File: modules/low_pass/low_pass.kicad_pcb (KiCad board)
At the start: 2 copper layers, 30.5 x 68.6 mm, 4 parts

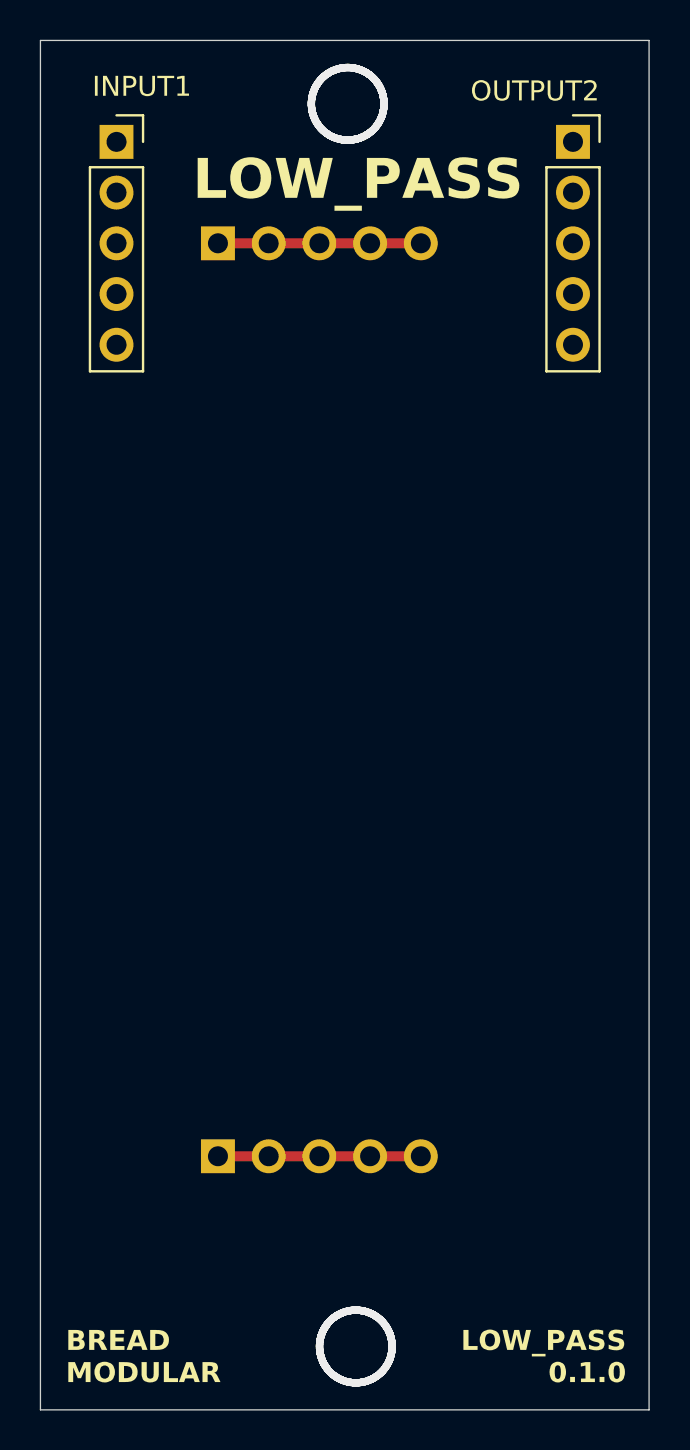
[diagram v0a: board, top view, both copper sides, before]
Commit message: layout components in the PCB
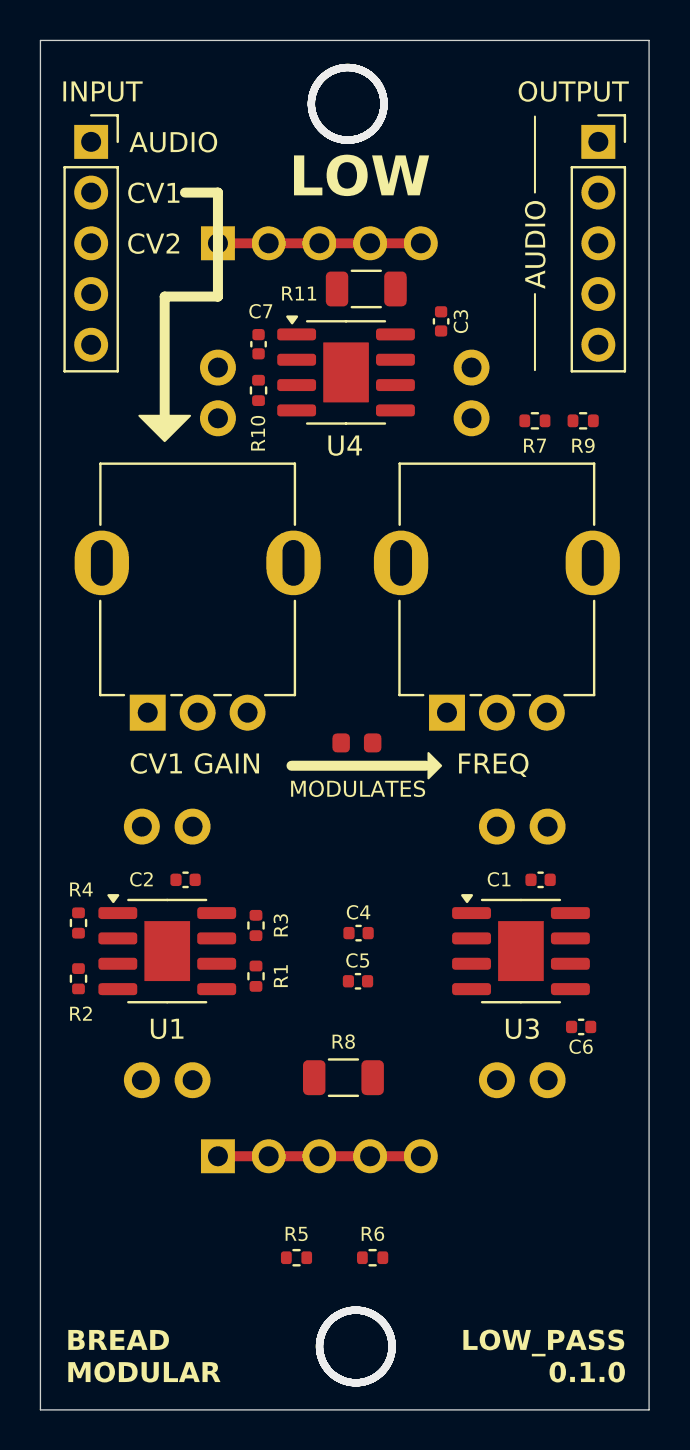
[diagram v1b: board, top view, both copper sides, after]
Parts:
- removed OUTPUT2: Conn_01x05_Socket, Connector_PinSocket_2.54mm:PinSocket_1x05_P2.54mm_Vertical
- added C1: 0.1uf, Capacitor_SMD:C_0402_1005Metric, F.Cu at (72.0, 82.7)
- added C2: 0.1uf, Capacitor_SMD:C_0402_1005Metric, F.Cu at (54.3, 82.7)
- added C3: 0.1uf, Capacitor_SMD:C_0402_1005Metric, F.Cu at (67.1, 54.7)
- added C4: 1nf, Capacitor_SMD:C_0402_1005Metric, F.Cu at (62.9, 85.3)
- added C5: 1nf, Capacitor_SMD:C_0402_1005Metric, F.Cu at (62.9, 87.8)
- added C6: 1nf, Capacitor_SMD:C_0402_1005Metric, F.Cu at (74.1, 90.0)
- added C7: 0.1uf, Capacitor_SMD:C_0402_1005Metric, F.Cu at (57.9, 55.9)
- added D1: LED, LED_SMD:LED_0603_1608Metric, F.Cu at (62.8, 75.8)
- added OUTPUT1: Conn_01x05_Socket, Connector_PinSocket_2.54mm:PinSocket_1x05_P2.54mm_Vertical, F.Cu at (74.9, 45.7)
- added R1: 100k, Resistor_SMD:R_0402_1005Metric, F.Cu at (57.8, 87.5)
- added R10: 100k, Resistor_SMD:R_0402_1005Metric, F.Cu at (57.9, 58.2)
- added R11: 330, Resistor_SMD:R_1206_3216Metric, F.Cu at (63.3, 53.1)
- added R2: 100k, Resistor_SMD:R_0402_1005Metric, F.Cu at (48.9, 87.6)
- added R3: 100k, Resistor_SMD:R_0402_1005Metric, F.Cu at (57.8, 85.0)
- added R4: 200k, Resistor_SMD:R_0402_1005Metric, F.Cu at (48.9, 84.8)
- added R5: 1k, Resistor_SMD:R_0402_1005Metric, F.Cu at (59.8, 101.6)
- added R6: 1k, Resistor_SMD:R_0402_1005Metric, F.Cu at (63.6, 101.6)
- added R7: 100k, Resistor_SMD:R_0402_1005Metric, F.Cu at (71.8, 59.7)
- added R8: 330, Resistor_SMD:R_1206_3216Metric, F.Cu at (62.2, 92.6)
- added R9: 1k, Resistor_SMD:R_0402_1005Metric, F.Cu at (74.2, 59.7)
- added RV1: 1M, BreadModular_Pots:Potentiometer_RV09, F.Cu at (52.4, 74.3)
- added RV2: 1M, BreadModular_Pots:Potentiometer_RV09, F.Cu at (67.3, 74.3)
- added U1: MCP6002-xSN, Package_SO:SOIC-8-1EP_3.9x4.9mm_P1.27mm_EP2.29x3mm, F.Cu at (53.3, 86.2)
- added U2: VTL5C, BreadModular_MISC:VTL5C, B.Cu at (71.1, 86.4)
- added U3: MCP6002-xSN, Package_SO:SOIC-8-1EP_3.9x4.9mm_P1.27mm_EP2.29x3mm, F.Cu at (71.1, 86.2)
- added U4: MCP6002-xSN, Package_SO:SOIC-8-1EP_3.9x4.9mm_P1.27mm_EP2.29x3mm, F.Cu at (62.3, 57.3)
- added U5: VTL5C, BreadModular_MISC:VTL5C, B.Cu at (53.3, 86.4)
- added U6: VTL5C, BreadModular_MISC:VTL5C, B.Cu at (62.2, 58.3)
- moved INPUT1 1.27 mm to (49.5, 45.7)
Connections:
- INPUT1 pad 1: unconnected-(INPUT1-Pin_1-Pad1) -> AUDIO_IN
- INPUT1 pad 2: unconnected-(INPUT1-Pin_2-Pad2) -> MOD_CV_IN
- INPUT1 pad 3: unconnected-(INPUT1-Pin_3-Pad3) -> CUTOFF_CV_IN
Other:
- board text added: "AUDIO"
- board text added: "CV1"
- board text added: "CV1 GAIN"
- board text added: "CV2"
- board text added: "FREQ"
- board text added: "INPUT"
- board text added: "LOW"
- board text added: "MODULATES"
- board text added: "OUTPUT"
- board text removed: "LOW_PASS"

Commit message: update pcb layout
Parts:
- moved U5 3.47 mm to (56.5, 85.0)
- moved U2 2.34 mm to (69.3, 84.8)
- moved D1 2.03 mm to (62.8, 77.9)
- moved R8 1.48 mm to (62.9, 91.3)
- moved U6 1.28 mm to (62.1, 59.6)
- moved R5 1.09 mm to (60.7, 101.0)
- moved R6 1.09 mm to (64.5, 101.0)
- moved C6 0.28 mm to (73.8, 89.9)
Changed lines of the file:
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@@
 	(footprint "Resistor_SMD:R_0402_1005Metric"
 		(layer "F.Cu")
-		(at 59.815 101.6)
+		(at 60.704 100.965)
 		(descr "Resistor SMD 0402 (1005 Metric), square (rectangular) end terminal, IPC_7351 nominal, (Body size source: IPC-SM-782 page 72, https://www.pcb-3d.com/wordpress/wp-content/uploads/ipc-sm-782a_amendment_1_and_2.pdf), generated with kicad-footprint-generator")
 		(tags "resistor")
@@
 		(tags "capacitor")
 		(property "Reference" "C1"
-			(at 2.06 0 360)
+			(at 2.06 0 0)
 			(layer "F.SilkS")
 			(effects
@@
 		)
 		(property "Value" "0.1uf"
-			(at 0 1.27 360)
+			(at 0 1.27 0)
 			(layer "F.Fab")
 			(effects
@@
 		)
 		(fp_text user "${REFERENCE}"
-			(at 0 0 360)
+			(at 0 0 0)
 			(layer "F.Fab")
 			(effects
@@
 		(tags "resistor")
 		(property "Reference" "R11"
-			(at -3.3635 0.254 360)
+			(at -3.3635 0.254 0)
 			(layer "F.SilkS")
 			(effects
@@
 		)
 		(property "Value" "330"
-			(at 0 1.82 360)
+			(at 0 1.82 0)
 			(layer "F.Fab")
 			(effects
@@
 		)
 		(fp_text user "${REFERENCE}"
-			(at 0 0 360)
+			(at 0 0 0)
 			(layer "F.Fab")
 			(effects
@@
 	(footprint "Resistor_SMD:R_0402_1005Metric"
 		(layer "F.Cu")
-		(at 63.625 101.6)
+		(at 64.514 100.965)
 		(descr "Resistor SMD 0402 (1005 Metric), square (rectangular) end terminal, IPC_7351 nominal, (Body size source: IPC-SM-782 page 72, https://www.pcb-3d.com/wordpress/wp-content/uploads/ipc-sm-782a_amendment_1_and_2.pdf), generated with kicad-footprint-generator")
 		(tags "resistor")
@@
 		(tags "SOIC SO")
 		(property "Reference" "U3"
-			(at 0.065 3.925 0)
+			(at 0.065 3.417 0)
 			(layer "F.SilkS")
 			(effects
@@
 		(tags "capacitor")
 		(property "Reference" "C2"
-			(at 2.187 0 360)
+			(at 2.187 0 0)
 			(layer "F.SilkS")
 			(effects
@@
 		)
 		(property "Value" "0.1uf"
-			(at 0 1.27 360)
+			(at 0 1.27 0)
 			(layer "F.Fab")
 			(effects
@@
 		)
 		(fp_text user "${REFERENCE}"
-			(at 0 0 360)
+			(at 0 0 0)
 			(layer "F.Fab")
 			(effects
@@
 	(footprint "Resistor_SMD:R_1206_3216Metric"
 		(layer "F.Cu")
-		(at 62.1645 92.583 180)
+		(at 62.9265 91.313 180)
 		(descr "Resistor SMD 1206 (3216 Metric), square (rectangular) end terminal, IPC_7351 nominal, (Body size source: IPC-SM-782 page 72, https://www.pcb-3d.com/wordpress/wp-content/uploads/ipc-sm-782a_amendment_1_and_2.pdf), generated with kicad-footprint-generator")
 		(tags "resistor")
 		(property "Reference" "R8"
-			(at 0 1.778 360)
+			(at 0 1.778 0)
 			(layer "F.SilkS")
 			(effects
@@
 		)
 		(property "Value" "330"
-			(at 0 1.82 360)
+			(at 0 1.82 0)
 			(layer "F.Fab")
 			(effects
@@
 		)
 		(fp_text user "${REFERENCE}"
-			(at 0 0 360)
+			(at 0 0 0)
 			(layer "F.Fab")
 			(effects
@@
 	(footprint "LED_SMD:LED_0603_1608Metric"
 		(layer "F.Cu")
-		(at 62.8395 75.819)
+		(at 62.8395 77.851)
 		(descr "LED SMD 0603 (1608 Metric), square (rectangular) end terminal, IPC_7351 nominal, (Body size source: http://www.tortai-tech.com/upload/download/2011102023233369053.pdf), generated with kicad-footprint-generator")
 		(tags "LED")
@@
 		(tags "SOIC SO")
 		(property "Reference" "U1"
-			(at 0 3.925 0)
+			(at 0 3.417 0)
 			(layer "F.SilkS")
 			(effects
@@
 	(footprint "Capacitor_SMD:C_0402_1005Metric"
 		(layer "F.Cu")
-		(at 74.069 90.043 180)
+		(at 73.815 89.916 180)
 		(descr "Capacitor SMD 0402 (1005 Metric), square (rectangular) end terminal, IPC_7351 nominal, (Body size source: IPC-SM-782 page 76, https://www.pcb-3d.com/wordpress/wp-content/uploads/ipc-sm-782a_amendment_1_and_2.pdf), generated with kicad-footprint-generator")
 		(tags "capacitor")
 		(property "Reference" "C6"
-			(at 0 -1.016 360)
+			(at 0 -1.016 0)
 			(layer "F.SilkS")
 			(effects
@@
 		)
 		(property "Value" "1nf"
-			(at 0 1.27 360)
+			(at 0 1.27 0)
 			(layer "F.Fab")
 			(effects
@@
 		)
 		(fp_text user "${REFERENCE}"
-			(at 0 0 360)
+			(at 0 0 0)
 			(layer "F.Fab")
 			(effects
@@
 	(footprint "BreadModular_MISC:VTL5C"
 		(layer "B.Cu")
-		(at 71.12 86.36)
+		(at 69.342 84.836)
 		(property "Reference" "U2"
 			(at 0 -8.89 180)
@@
 	(footprint "BreadModular_MISC:VTL5C"
 		(layer "B.Cu")
-		(at 62.23 58.293 90)
+		(at 62.103 59.563 90)
 		(property "Reference" "U6"
 			(at 0 -8.89 -90)
@@
 	(footprint "BreadModular_MISC:VTL5C"
 		(layer "B.Cu")
-		(at 53.34 86.36)
+		(at 56.515 84.963)
 		(property "Reference" "U5"
 			(at 0 -8.89 180)
@@
 		(layer "F.SilkS")
 	)
+	(gr_poly
+		(pts
+			(xy 67.056 76.581) (xy 65.786 77.851) (xy 65.786 75.311)
+		)
+		(stroke
+			(width 0.1)
+			(type solid)
+		)
+		(fill solid)
+		(layer "F.SilkS")
+	)
 	(gr_line
 		(start 71.755 53.34)
@@
 	)
 	(gr_line
-		(start 59.563 76.962)
-		(end 66.294 76.962)
+		(start 59.563 76.581)
+		(end 66.294 76.581)
 		(stroke
 			(width 0.5)
@@
 	(gr_poly
 		(pts
-			(xy 67.056 76.962) (xy 66.421 76.327) (xy 66.421 77.597)
+			(xy 67.056 76.581) (xy 66.421 75.946) (xy 66.421 77.216)
 		)
 		(stroke
@@
 	)
 	(gr_text "FREQ"
-		(at 67.818 77.47 0)
+		(at 67.818 77.216 0)
 		(layer "F.SilkS")
 		(effects
@@
 	)
 	(gr_text "CV1 GAIN"
-		(at 51.435 77.47 0)
+		(at 51.435 77.216 0)
 		(layer "F.SilkS")
 		(effects
@@
 	)
 	(gr_text "MODULATES"
-		(at 59.436 78.613 0)
+		(at 59.69 79.756 0)
 		(layer "F.SilkS")
 		(effects
 			(font
-				(size 0.8 0.8)
+				(size 0.75 0.75)
 				(thickness 0.1)
 			)

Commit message: Finalized the PCB design
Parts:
- moved R5 0.76 mm to (60.7, 100.2)
- moved R6 0.76 mm to (64.5, 100.2)
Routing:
- net GND: track 10.2 -> 167.5 mm, vias 0 -> 9
- net +5V: track 10.2 -> 144.8 mm, vias 0 -> 4
- net +2.5V: track 0.00 -> 97.3 mm, vias 0 -> 4
- net AUDIO_IN: track 0.00 -> 75.7 mm
- net Net-(U3B--): track 0.00 -> 56.1 mm, vias 0 -> 4
- net Net-(U3B-+): track 0.00 -> 51.5 mm, vias 0 -> 2
- net Net-(U5-+): track 0.00 -> 47.5 mm, vias 0 -> 3
- net PROCESSED_MOD_CV: track 0.00 -> 46.1 mm, vias 0 -> 2
- net Net-(U2-+): track 0.00 -> 40.5 mm, vias 0 -> 2
- net Net-(D1-A): track 0.00 -> 36.0 mm
- net Net-(D1-K): track 0.00 -> 35.4 mm
- net Net-(C4-Pad1): track 0.00 -> 32.3 mm, vias 0 -> 1
- net CUTOFF_CV_IN: track 0.00 -> 30.8 mm, vias 0 -> 2
- net MOD_CV_IN: track 0.00 -> 28.3 mm
- net Net-(R1-Pad1): track 0.00 -> 24.1 mm
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
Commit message: Finalized low_pass
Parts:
- R11, R8: footprint Resistor_SMD:R_1206_3216Metric -> Resistor_SMD:R_0805_2012Metric
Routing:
- net Net-(R8-Pad1): track 20.5 -> 22.8 mm
- net Net-(U5-+): track 47.5 -> 48.5 mm
- net Net-(D1-K): track 35.4 -> 35.9 mm
- net GND: track 167.5 -> 168.1 mm
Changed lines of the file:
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@@
 		)
 	)
-	(footprint "Resistor_SMD:R_1206_3216Metric"
+	(footprint "Resistor_SMD:R_0805_2012Metric"
 		(layer "F.Cu")
 		(at 63.3075 53.086)
-		(descr "Resistor SMD 1206 (3216 Metric), square (rectangular) end terminal, IPC_7351 nominal, (Body size source: IPC-SM-782 page 72, https://www.pcb-3d.com/wordpress/wp-content/uploads/ipc-sm-782a_amendment_1_and_2.pdf), generated with kicad-footprint-generator")
+		(descr "Resistor SMD 0805 (2012 Metric), square (rectangular) end terminal, IPC_7351 nominal, (Body size source: IPC-SM-782 page 72, https://www.pcb-3d.com/wordpress/wp-content/uploads/ipc-sm-782a_amendment_1_and_2.pdf), generated with kicad-footprint-generator")
 		(tags "resistor")
 		(property "Reference" "R11"
-			(at -3.3635 0.254 0)
+			(at -2.9825 0 0)
 			(layer "F.SilkS")
 			(effects
@@
 		)
 		(property "Value" "330"
-			(at 0 1.82 0)
+			(at 0 1.65 0)
 			(layer "F.Fab")
 			(effects
 				(font
-					(size 0.7 0.7)
-					(thickness 0.1)
+					(size 1 1)
+					(thickness 0.15)
 				)
 			)
 		)
-		(property "Footprint" "Resistor_SMD:R_1206_3216Metric"
+		(property "Footprint" "Resistor_SMD:R_0805_2012Metric"
 			(at 0 0 0)
 			(unlocked yes)
@@
 		(attr smd)
 		(fp_line
-			(start -0.727064 -0.91)
-			(end 0.727064 -0.91)
+			(start -0.227064 -0.735)
+			(end 0.227064 -0.735)
 			(stroke
 				(width 0.12)
@@
 		)
 		(fp_line
-			(start -0.727064 0.91)
-			(end 0.727064 0.91)
+			(start -0.227064 0.735)
+			(end 0.227064 0.735)
 			(stroke
 				(width 0.12)
@@
 		)
 		(fp_line
-			(start -2.28 -1.12)
-			(end 2.28 -1.12)
+			(start -1.68 -0.95)
+			(end 1.68 -0.95)
 			(stroke
 				(width 0.05)
@@
 		)
 		(fp_line
-			(start -2.28 1.12)
-			(end -2.28 -1.12)
+			(start -1.68 0.95)
+			(end -1.68 -0.95)
 			(stroke
 				(width 0.05)
@@
 		)
 		(fp_line
-			(start 2.28 -1.12)
-			(end 2.28 1.12)
+			(start 1.68 -0.95)
+			(end 1.68 0.95)
 			(stroke
 				(width 0.05)
@@
 		)
 		(fp_line
-			(start 2.28 1.12)
-			(end -2.28 1.12)
+			(start 1.68 0.95)
+			(end -1.68 0.95)
 			(stroke
 				(width 0.05)
@@
 		)
 		(fp_line
-			(start -1.6 -0.8)
-			(end 1.6 -0.8)
+			(start -1 -0.625)
+			(end 1 -0.625)
 			(stroke
 				(width 0.1)
@@
 		)
 		(fp_line
-			(start -1.6 0.8)
-			(end -1.6 -0.8)
+			(start -1 0.625)
+			(end -1 -0.625)
 			(stroke
 				(width 0.1)
@@
 		)
 		(fp_line
-			(start 1.6 -0.8)
-			(end 1.6 0.8)
+			(start 1 -0.625)
+			(end 1 0.625)
 			(stroke
 				(width 0.1)
@@
 		)
 		(fp_line
-			(start 1.6 0.8)
-			(end -1.6 0.8)
+			(start 1 0.625)
+			(end -1 0.625)
 			(stroke
 				(width 0.1)
@@
 			(effects
 				(font
-					(size 0.7 0.7)
-					(thickness 0.1)
+					(size 0.5 0.5)
+					(thickness 0.08)
 				)
 			)
 		)
 		(pad "1" smd roundrect
-			(at -1.4625 0)
-			(size 1.125 1.75)
+			(at -0.9125 0)
+			(size 1.025 1.4)
 			(layers "F.Cu" "F.Paste" "F.Mask")
-			(roundrect_rratio 0.222222)
+			(roundrect_rratio 0.243902)
 			(net 10 "Net-(D1-K)")
 			(pintype "passive")
 		)
 		(pad "2" smd roundrect
-			(at 1.4625 0)
-			(size 1.125 1.75)
+			(at 0.9125 0)
+			(size 1.025 1.4)
 			(layers "F.Cu" "F.Paste" "F.Mask")
-			(roundrect_rratio 0.222222)
+			(roundrect_rratio 0.243902)
 			(net 1 "GND")
 			(pintype "passive")
 		)
-		(model "${KICAD8_3DMODEL_DIR}/Resistor_SMD.3dshapes/R_1206_3216Metric.wrl"
+		(model "${KICAD8_3DMODEL_DIR}/Resistor_SMD.3dshapes/R_0805_2012Metric.wrl"
 			(offset
 				(xyz 0 0 0)
@@
 		)
 	)
-	(footprint "Resistor_SMD:R_1206_3216Metric"
+	(footprint "Resistor_SMD:R_0805_2012Metric"
 		(layer "F.Cu")
 		(at 62.9265 91.313 180)
-		(descr "Resistor SMD 1206 (3216 Metric), square (rectangular) end terminal, IPC_7351 nominal, (Body size source: IPC-SM-782 page 72, https://www.pcb-3d.com/wordpress/wp-content/uploads/ipc-sm-782a_amendment_1_and_2.pdf), generated with kicad-footprint-generator")
+		(descr "Resistor SMD 0805 (2012 Metric), square (rectangular) end terminal, IPC_7351 nominal, (Body size source: IPC-SM-782 page 72, https://www.pcb-3d.com/wordpress/wp-content/uploads/ipc-sm-782a_amendment_1_and_2.pdf), generated with kicad-footprint-generator")
 		(tags "resistor")
 		(property "Reference" "R8"
-			(at 0 1.778 0)
+			(at 0 -1.65 180)
 			(layer "F.SilkS")
 			(effects
 				(font
-					(size 0.7 0.7)
-					(thickness 0.1)
+					(size 1 1)
+					(thickness 0.15)
 				)
 			)
 		)
 		(property "Value" "330"
-			(at 0 1.82 0)
+			(at 0 1.65 180)
 			(layer "F.Fab")
 			(effects
 				(font
-					(size 0.7 0.7)
-					(thickness 0.1)
+					(size 1 1)
+					(thickness 0.15)
 				)
 			)
 		)
-		(property "Footprint" "Resistor_SMD:R_1206_3216Metric"
+		(property "Footprint" "Resistor_SMD:R_0805_2012Metric"
 			(at 0 0 180)
 			(unlocked yes)
@@
 		(attr smd)
 		(fp_line
-			(start -0.727064 0.91)
-			(end 0.727064 0.91)
+			(start -0.227064 0.735)
+			(end 0.227064 0.735)
 			(stroke
 				(width 0.12)
@@
 		)
 		(fp_line
-			(start -0.727064 -0.91)
-			(end 0.727064 -0.91)
+			(start -0.227064 -0.735)
+			(end 0.227064 -0.735)
 			(stroke
 				(width 0.12)
@@
 		)
 		(fp_line
-			(start 2.28 1.12)
-			(end -2.28 1.12)
+			(start 1.68 0.95)
+			(end -1.68 0.95)
 			(stroke
 				(width 0.05)
@@
 		)
 		(fp_line
-			(start 2.28 -1.12)
-			(end 2.28 1.12)
+			(start 1.68 -0.95)
+			(end 1.68 0.95)
 			(stroke
 				(width 0.05)
@@
 		)
 		(fp_line
-			(start -2.28 1.12)
-			(end -2.28 -1.12)
+			(start -1.68 0.95)
+			(end -1.68 -0.95)
 			(stroke
 				(width 0.05)
@@
 		)
 		(fp_line
-			(start -2.28 -1.12)
-			(end 2.28 -1.12)
+			(start -1.68 -0.95)
+			(end 1.68 -0.95)
 			(stroke
 				(width 0.05)
@@
 		)
 		(fp_line
-			(start 1.6 0.8)
-			(end -1.6 0.8)
+			(start 1 0.625)
+			(end -1 0.625)
 			(stroke
 				(width 0.1)
@@
 		)
 		(fp_line
-			(start 1.6 -0.8)
-			(end 1.6 0.8)
+			(start 1 -0.625)
+			(end 1 0.625)
 			(stroke
 				(width 0.1)
@@
 		)
 		(fp_line
-			(start -1.6 0.8)
-			(end -1.6 -0.8)
+			(start -1 0.625)
+			(end -1 -0.625)
 			(stroke
 				(width 0.1)
@@
 		)
 		(fp_line
-			(start -1.6 -0.8)
-			(end 1.6 -0.8)
+			(start -1 -0.625)
+			(end 1 -0.625)
 			(stroke
 				(width 0.1)
@@
 		)
 		(fp_text user "${REFERENCE}"
-			(at 0 0 0)
+			(at 0 0 180)
 			(layer "F.Fab")
 			(effects
 				(font
-					(size 0.7 0.7)
-					(thickness 0.1)
+					(size 0.5 0.5)
+					(thickness 0.08)
 				)
 			)
 		)
 		(pad "1" smd roundrect
-			(at -1.4625 0 180)
-			(size 1.125 1.75)
+			(at -0.9125 0 180)
+			(size 1.025 1.4)
 			(layers "F.Cu" "F.Paste" "F.Mask")
-			(roundrect_rratio 0.222222)
+			(roundrect_rratio 0.243902)
 			(net 24 "Net-(R8-Pad1)")
 			(pintype "passive")
 		)
 		(pad "2" smd roundrect
-			(at 1.4625 0 180)
-			(size 1.125 1.75)
+			(at 0.9125 0 180)
+			(size 1.025 1.4)
 			(layers "F.Cu" "F.Paste" "F.Mask")
-			(roundrect_rratio 0.222222)
+			(roundrect_rratio 0.243902)
 			(net 23 "Net-(U5-+)")
 			(pintype "passive")
 		)
-		(model "${KICAD8_3DMODEL_DIR}/Resistor_SMD.3dshapes/R_1206_3216Metric.wrl"
+		(model "${KICAD8_3DMODEL_DIR}/Resistor_SMD.3dshapes/R_0805_2012Metric.wrl"
 			(offset
 				(xyz 0 0 0)
@@
 	)
 	(segment
+		(start 66.294 53.086)
+		(end 64.22 53.086)
+		(width 0.5)
+		(layer "F.Cu")
+		(net 1)
+	)
+	(segment
 		(start 55.88 96.52)
 		(end 66.04 96.52)
@@
 	)
 	(segment
-		(start 64.77 53.086)
-		(end 66.294 53.086)
-		(width 0.5)
-		(layer "F.Cu")
-		(net 1)
-	)
-	(segment
 		(start 59.69 59.3)
 		(end 59.82 59.17)
@@
 	)
 	(segment
-		(start 54.991 53.086)
-		(end 61.845 53.086)
+		(start 62.395 53.086)
+		(end 54.991 53.086)
 		(width 0.3)
 		(layer "F.Cu")
@@
 	)
 	(segment
-		(start 68.453 68.707)
-		(end 66.675 70.485)
+		(start 60.579 90.428)
+		(end 59.813 89.662)
 		(width 0.3)
 		(layer "F.Cu")
@@
 	)
 	(segment
-		(start 61.464 91.313)
-		(end 59.813 89.662)
+		(start 68.453 68.707)
+		(end 66.675 70.485)
 		(width 0.3)
 		(layer "F.Cu")
@@
 	)
 	(segment
+		(start 62.014 91.313)
+		(end 60.579 91.313)
+		(width 0.3)
+		(layer "F.Cu")
+		(net 23)
+	)
+	(segment
+		(start 60.579 91.313)
+		(end 60.579 90.428)
+		(width 0.3)
+		(layer "F.Cu")
+		(net 23)
+	)
+	(segment
 		(start 64.77 72.39)
 		(end 64.77 81.28)
@@
 	)
 	(segment
-		(start 64.389 91.313)
-		(end 64.389 85.217)
+		(start 65.54 90.686)
+		(end 64.262 89.408)
+		(width 0.3)
+		(layer "F.Cu")
+		(net 24)
+	)
+	(segment
+		(start 65.54 91.313)
+		(end 65.54 90.686)
+		(width 0.3)
+		(layer "F.Cu")
+		(net 24)
+	)
+	(segment
+		(start 63.839 91.313)
+		(end 65.54 91.313)
 		(width 0.3)
 		(layer "F.Cu")
@@
 	)
 	(segment
+		(start 64.262 85.344)
+		(end 64.389 85.217)
+		(width 0.3)
+		(layer "F.Cu")
+		(net 24)
+	)
+	(segment
 		(start 72.35 74.305)
 		(end 72.35 76.748)
 		(width 0.3)
 		(layer "F.Cu")
+		(net 24)
+	)
+	(segment
+		(start 64.262 89.408)
+		(end 64.262 85.344)
+		(width 0.3)
+		(layer "F.Cu")
